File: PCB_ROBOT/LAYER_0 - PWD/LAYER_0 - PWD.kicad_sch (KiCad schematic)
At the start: 11 parts, among them J1 PRIMARY IN, J2 SECONDARY IN

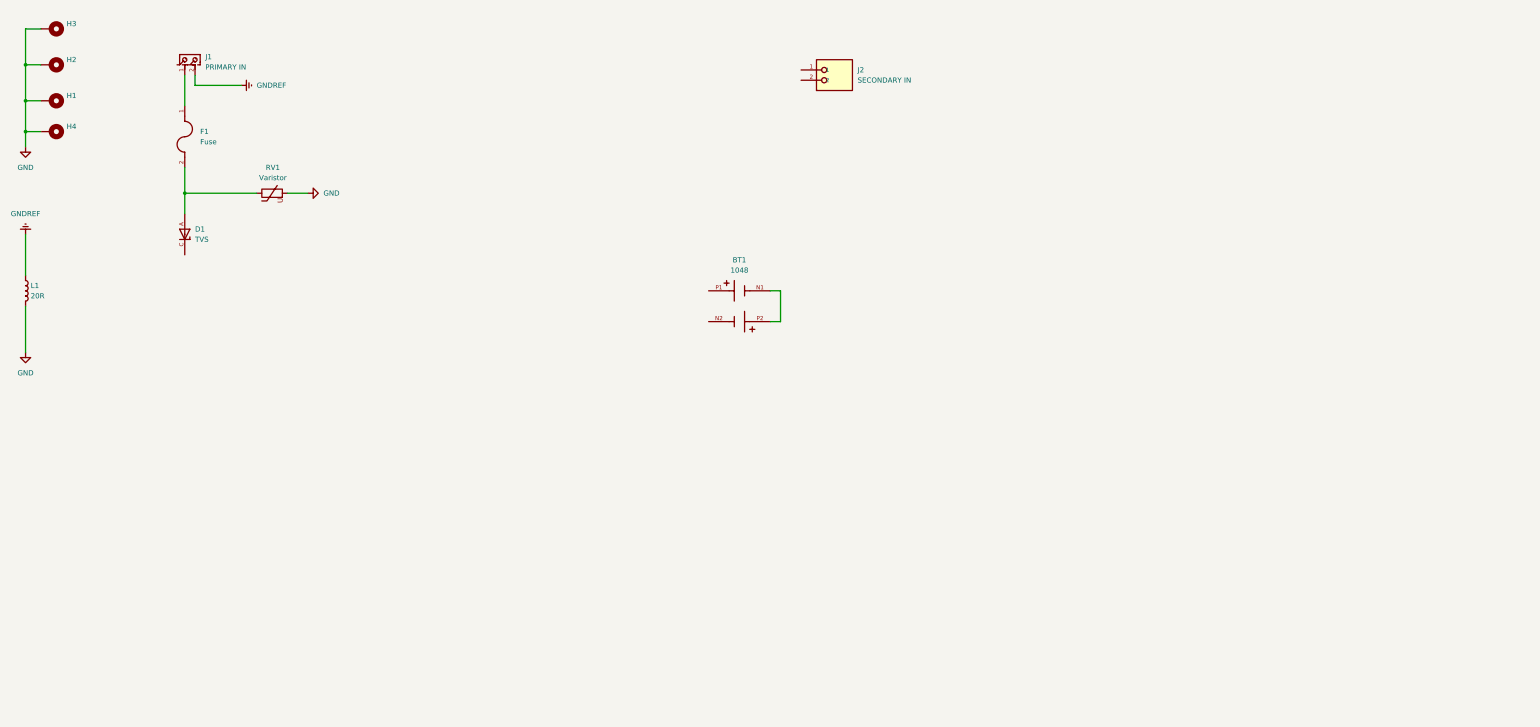
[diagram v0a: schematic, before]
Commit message: 5v Integration
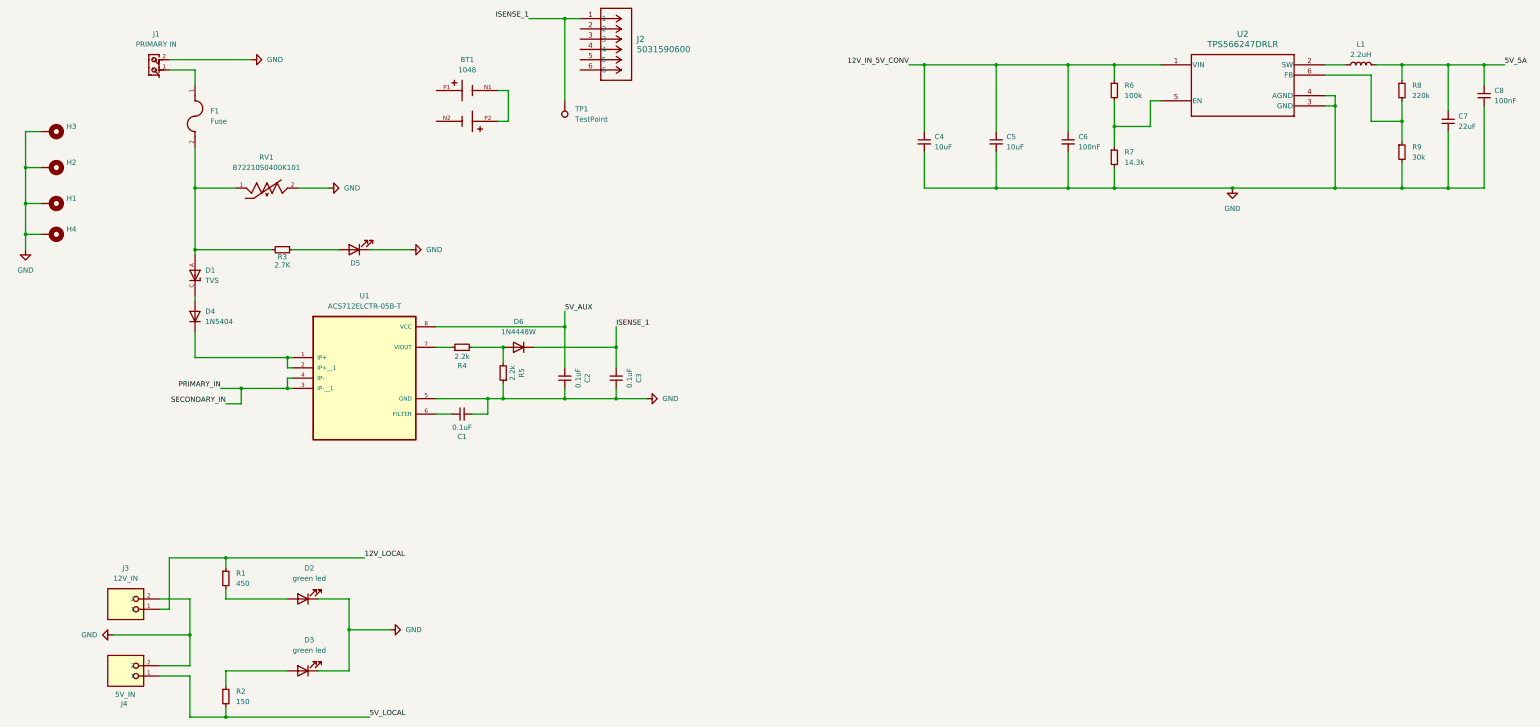
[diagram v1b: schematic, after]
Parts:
- removed J2: SECONDARY IN, 1984963:PHOENIX_1984963, symbol 1984963:1984963
- removed RV1: Varistor, symbol Device:Varistor
- added C1, C2, C3: 0.1uF, Capacitor_SMD:C_0603_1608Metric, symbol Device:C_Small
- added C4, C5: 10uF, symbol Device:C_Small
- added C6, C8: 100nF, symbol Device:C_Small
- added C7: 22uF, symbol Device:C_Small
- added D2, D3: green led, LED_SMD:LED_0805_2012Metric, symbol Device:LED
- added D4: 1N5404, Diode_THT:D_DO-201AD_P15.24mm_Horizontal, symbol Diode:1N5404
- added D5: LED, LED_SMD:LED_0805_2012Metric, symbol Device:LED
- added D6: 1N4448W, Diode_SMD:D_SOD-123, symbol Diode:1N4448W
- added J2: 5031590600, Footprints:CON_5031590600_MOL, symbol 5031590600:5031590600
- added J3: 12V_IN, Footprints:PHOENIX_1984963, symbol 1984963:1984963
- added J4: 5V_IN, Footprints:PHOENIX_1984963, symbol 1984963:1984963
- added R1: 450, Resistor_SMD:R_1206_3216Metric, symbol Device:R_Small
- added R2: 150, Resistor_SMD:R_1206_3216Metric, symbol Device:R_Small
- added R3: 2.7K, Resistor_SMD:R_1206_3216Metric, symbol Device:R_Small
- added R4, R5: 2.2k, Resistor_SMD:R_0603_1608Metric, symbol Device:R_Small
- added R6: 100k, symbol Device:R_Small
- added R7: 14.3k, symbol Device:R_Small
- added R8: 220k, symbol Device:R_Small
- added R9: 30k, symbol Device:R_Small
- added RV1: B72210S0400K101, Footprints:VAR_B72210S0400K101, symbol B72210S0400K101:B72210S0400K101
- added TP1: TestPoint, TestPoint:TestPoint_Pad_D1.5mm, symbol Connector:TestPoint
- added U1: ACS712ELCTR-05B-T, Footprints:SOIC127P600X175-8N, symbol ACS712ELCTR-05B-T:ACS712ELCTR-05B-T
- added U2: TPS566247DRLR, SOT-5X3-6_DRL_TEX, symbol TPS566247DRLR:TPS566247DRLR
- D1: footprint SMCJ58A:DIOM7959X262N -> Footprints:DIOM7959X262N
- F1: footprint 0679H3000-05:FUSC6125X279N -> Footprints:FUSC6125X279N
- L1: value 20R -> 2.2uH
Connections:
- net GND: now also J1.2, C1.2, C2.1, C3.1, C4.2, C5.2, C6.2, C7.2, C8.2, D2.1 (K), D3.1 (K), D5.1 (K), J3.2, J4.2, R5.1, R7.2, R9.2, RV1.2, U1.5 (GND), U2.3 (GND), U2.4 (AGND); no longer L1.2
- net at D1.A, F1.2: now also R3.2, RV1.1
- net at D1.C: now also D4.2 (A)
- net GNDREF: no longer names the net of L1.1
- net GNDREF: now also U2.2 (SW); no longer J1.2
- new net: D5.2 (A), R3.1
- new net: R6.2, R7.1, U2.5 (EN)
- new net: R8.2, R9.1, U2.6 (FB)
- new net: D4.1 (K), U1.1 (IP+), U1.2 (IP+__1)
- new net: D2.2 (A), R1.2
- new net: R4.1, U1.7 (VIOUT)
- new net: D6.2 (A), R4.2, R5.2
- new net: C1.1, U1.6 (FILTER)
- new net: D3.2 (A), R2.1
- new net 12V_IN_5V_CONV: C4.1, C5.1, C6.1, R6.1, U2.1 (VIN)
- new net 12V_LOCAL: J3.1, R1.1
- new net 5V_5A: C7.1, C8.1, L1.2, R8.1
- new net 5V_AUX: C2.2, U1.8 (VCC)
- new net 5V_LOCAL: J4.1, R2.2
- new net ISENSE_1: C3.2, D6.1 (K), J2.1, TP1.1
- new net PRIMARY_IN: U1.3 (IP-__1), U1.4 (IP-)
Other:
- moved on the sheet: BT1, D1, F1, H1, H2, H3, H4, J1
